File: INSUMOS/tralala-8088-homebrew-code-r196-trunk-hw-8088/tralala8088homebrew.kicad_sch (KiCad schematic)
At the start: 5 parts, among them U1 74HCT00

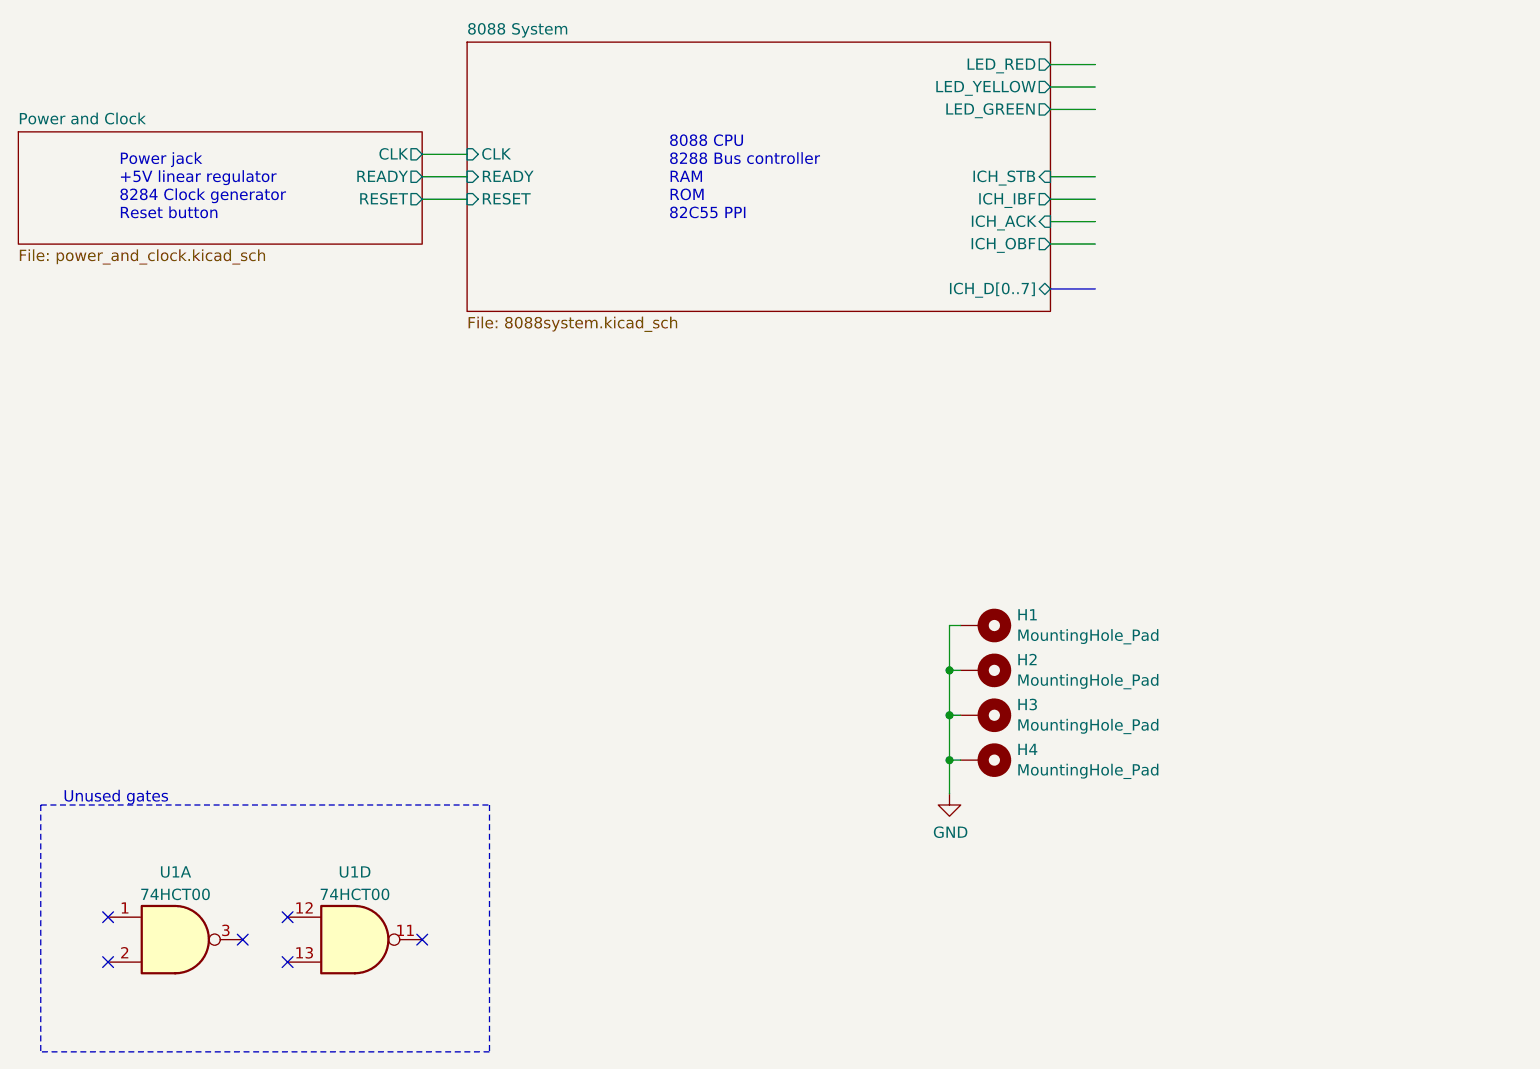
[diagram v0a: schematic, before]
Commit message: Inicio da bios apos testes
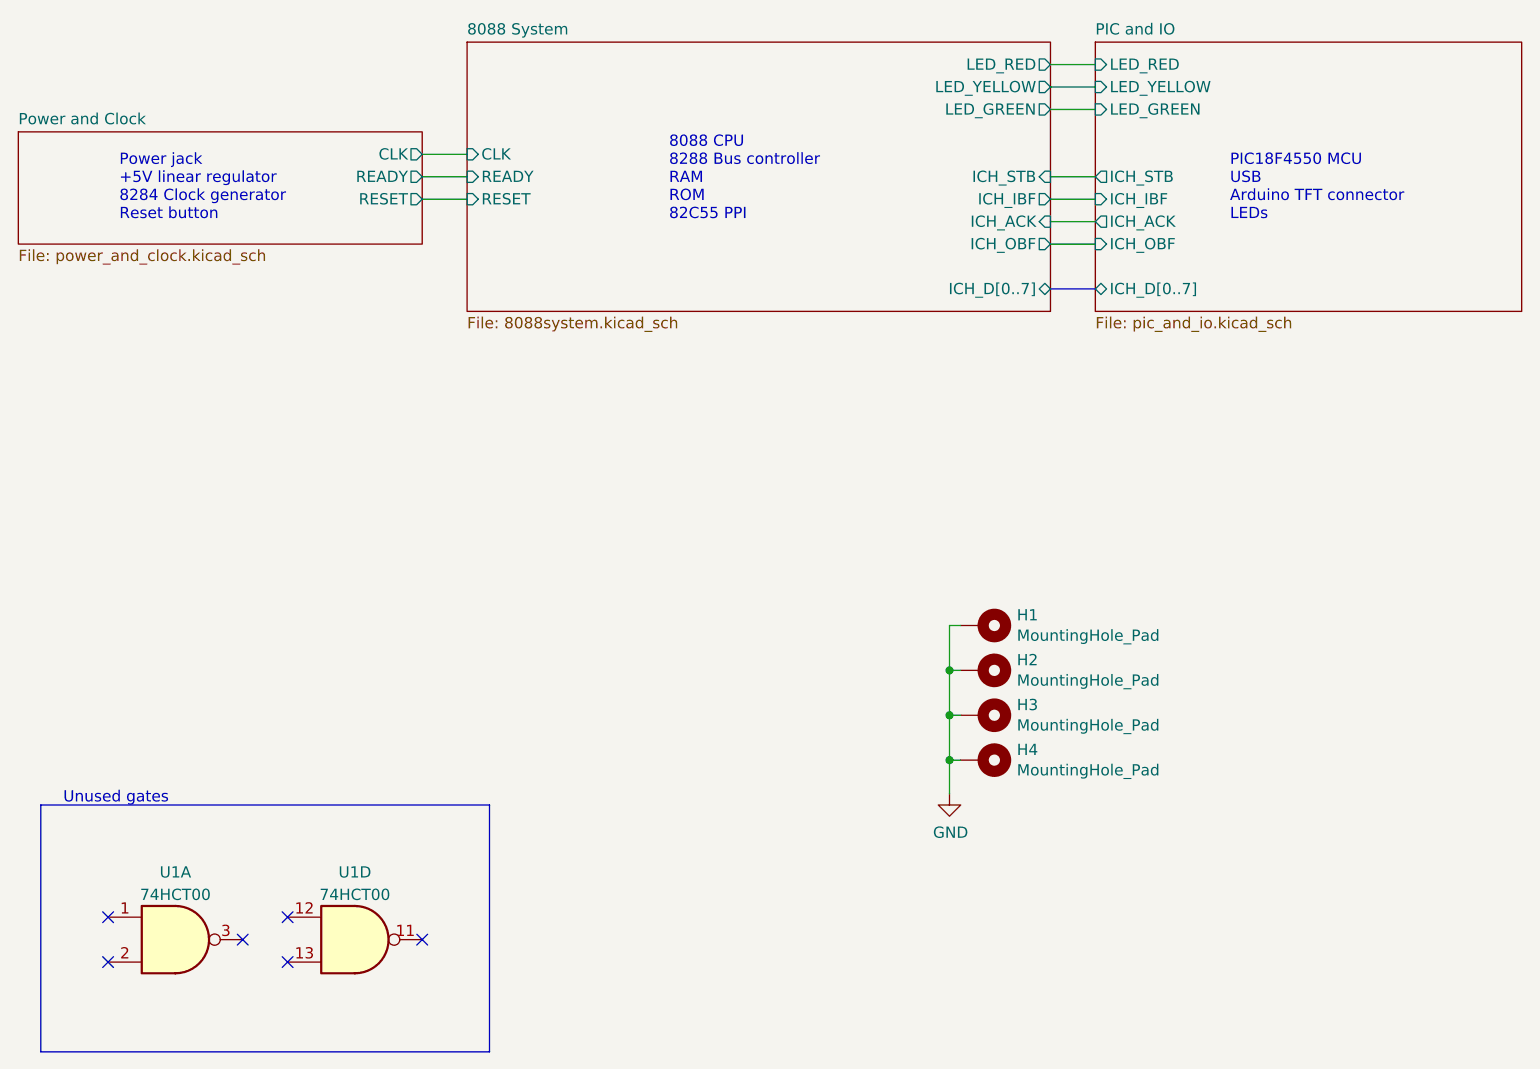
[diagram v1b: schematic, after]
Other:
- added sheet PIC and IO (pic_and_io.kicad_sch)
- note added: "PIC18F4550 MCU USB Arduino TFT connector LEDs"
